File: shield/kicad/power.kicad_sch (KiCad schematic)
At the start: 89 parts, among them J1 USB_Micro-B, J2 Battery, J3 J3, J4 J4, J5 J5, J6 Conn_01x03, J7 PWR_GOOD, Q1 NTR4101PT1G, Q2 DMG1012T, Q3 DMG1012T, Q4 NTR4101PT1G, Q5 DMG1012T, Q6 DMG1012T, SW1 SW_Push, SW2 SW_SPDT, U1 BQ25060, U2 TPS3422, U3 STC3100, U4 TPS63060, U5 MAX803

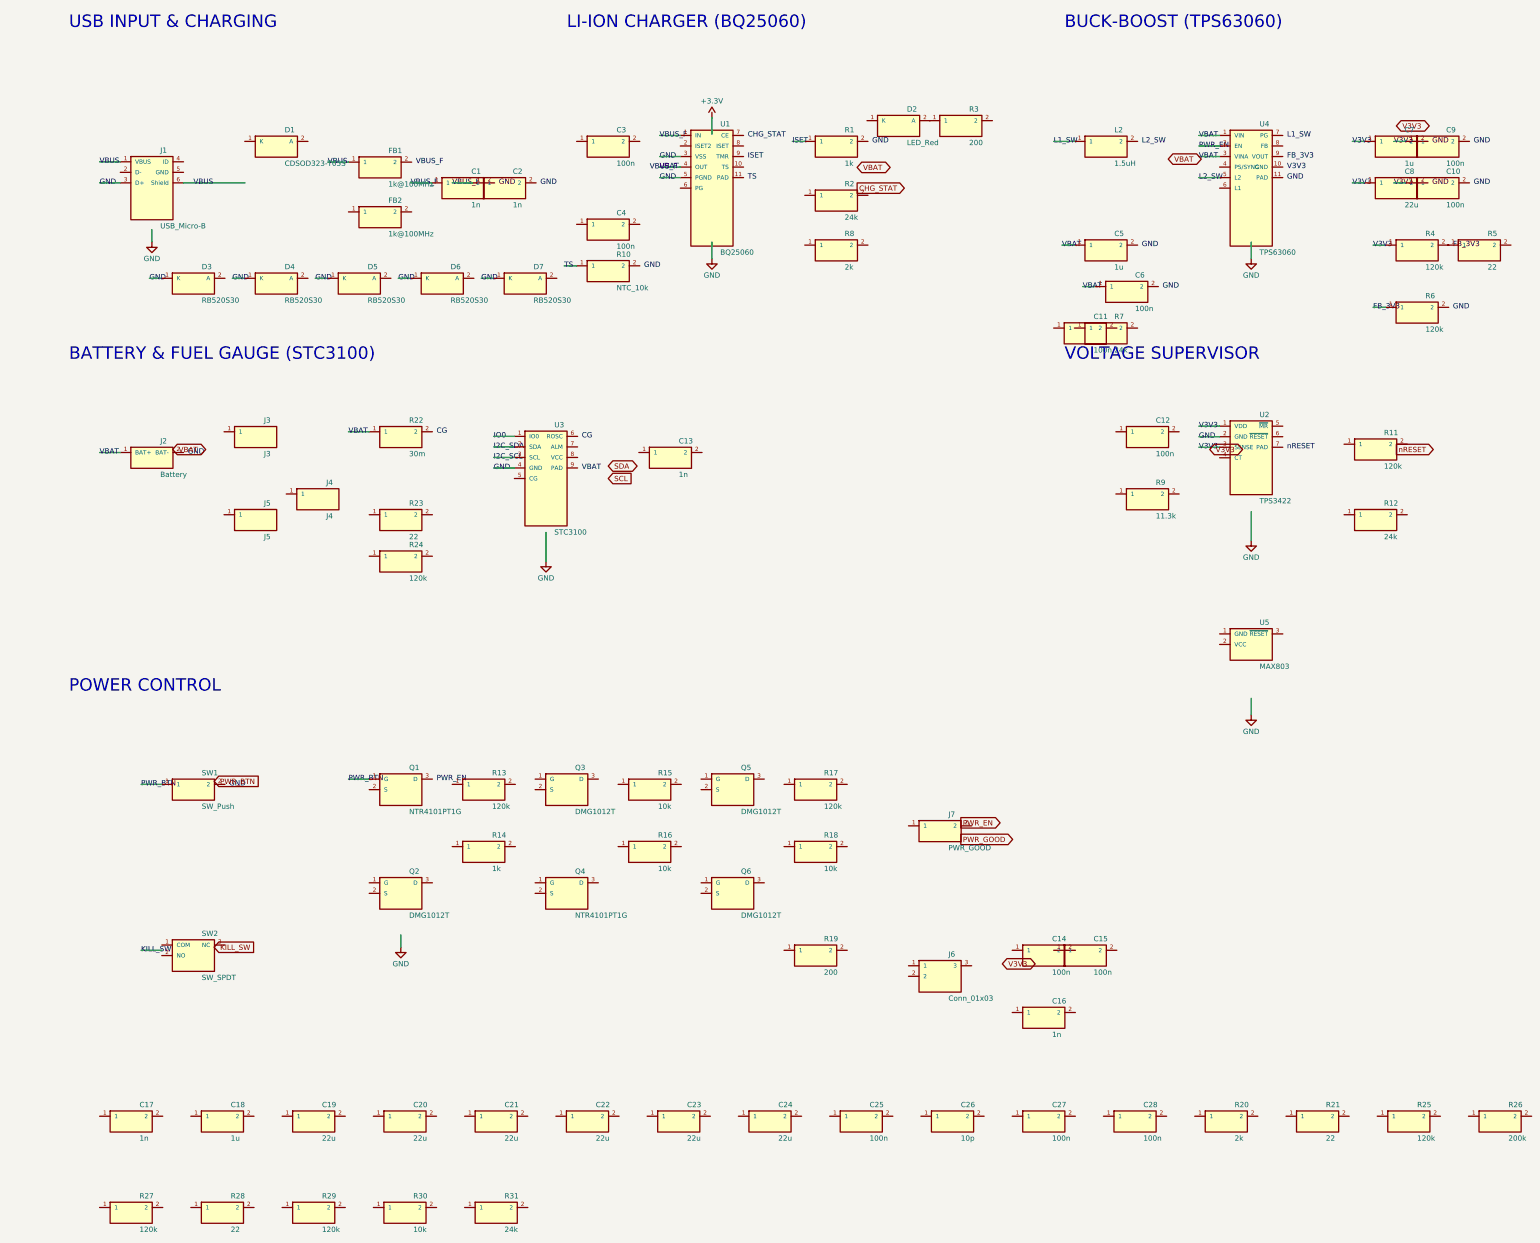
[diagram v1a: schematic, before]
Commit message: Add descriptive text blocks to all schematic sheets describing functional blocks
- Main sheet: board overview, sub-sheet summaries, and design notes
- Power sheet: USB input, charger, fuel gauge, buck-boost, supervisor, power control descriptions
- Peripherals sheet: smartcard, QR scanner, Arduino headers, buzzer, bypass descriptions
- Re-rendered all schematic and PCB images with kicad-cli-nightly

Agent-Logs-Url: https://github.com/3rdIteration/specter-diy/sessions/73613ef4-1004-4e39-bea0-e2793e248b2a

Co-authored-by: 3rdIteration <2230318+3rdIteration@users.noreply.github.com>
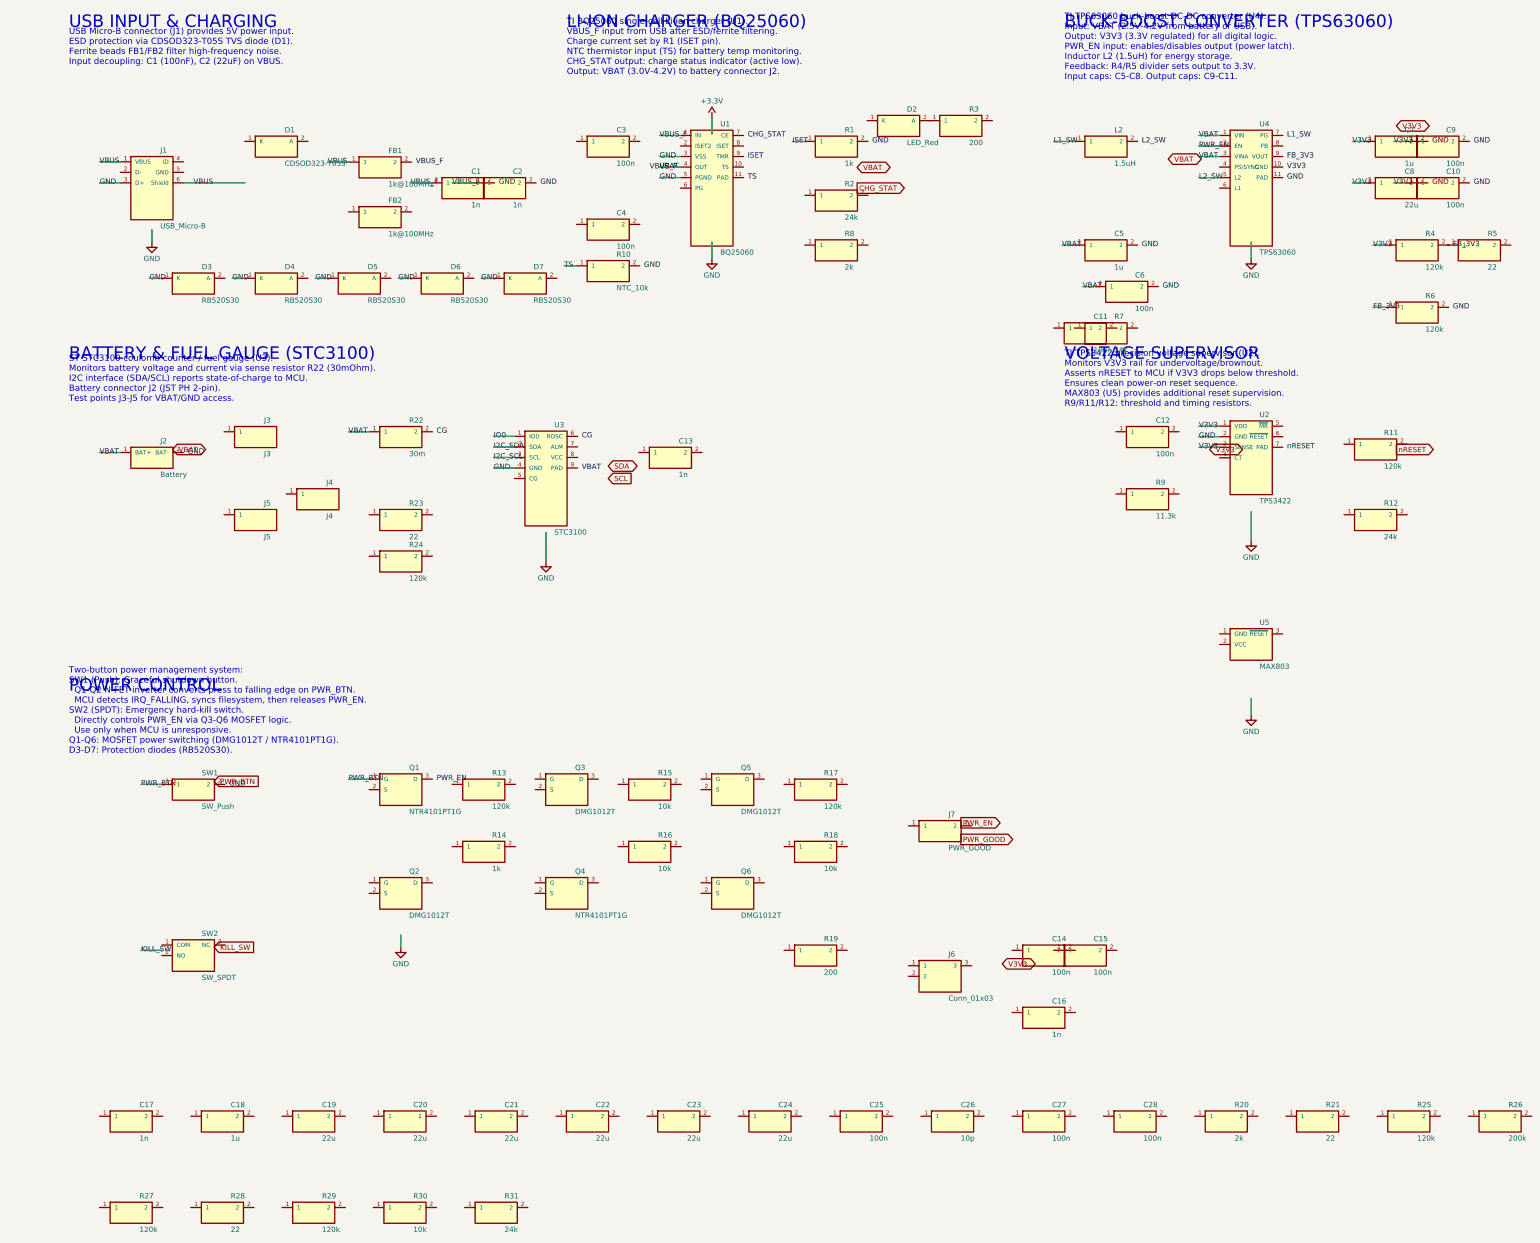
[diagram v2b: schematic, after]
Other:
- note added: "BUCK-BOOST CONVERTER (TPS63060)"
- note added: "ST STC3100 coulomb counter / fuel gauge (U3). Monitors battery voltage and current via sense resistor R22 (30mOhm). I2C interface (SDA/SCL) reports state-of-charge to MCU. Battery connector J2 (JST PH 2-pin). Test points J3-J5 for VBAT/GND access."
- note added: "TI BQ25060 single-cell Li-ion charger (U1). VBUS_F input from USB after ESD/ferrite filtering. Charge current set by R1 (ISET pin). NTC thermistor input (TS) for battery temp monitoring. CHG_STAT output: charge status indicator (active low). Output: VBAT (3.0V-4.2V) to battery connector J2."
- note added: "TI TPS3422 precision voltage supervisor (U2). Monitors V3V3 rail for undervoltage/brownout. Asserts nRESET to MCU if V3V3 drops below threshold. Ensures clean power-on reset sequence. MAX803 (U5) provides additional reset supervision. R9/R11/R12: threshold and timing resistors."
- note added: "TI TPS63060 buck-boost DC-DC converter (U4). Input: VBAT (2.5V-4.2V from battery or USB). Output: V3V3 (3.3V regulated) for all digital logic. PWR_EN input: enables/disables output (power latch). Inductor L2 (1.5uH) for energy storage. Feedback: R4/R5 divider sets output to 3.3V. Input caps: C5-C8. Output caps: C9-C11."
- note added: "Two-button power management system: SW1 (Push): Graceful shutdown button. Q1-Q2 N-FET inverter converts press to falling edge on PWR_BTN. MCU detects IRQ_FALLING, syncs filesystem, then releases PWR_EN. SW2 (SPDT): Emergency hard-kill switch. Directly controls PWR_EN via Q3-Q6 MOSFET logic. Use only when MCU is unresponsive. Q1-Q6: MOSFET power switching (DMG1012T / NTR4101PT1G). D3-D7: Protectio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"
- note added: "USB Micro-B connector (J1) provides 5V power input. ESD protection via CDSOD323-T05S TVS diode (D1). Ferrite beads FB1/FB2 filter high-frequency noise. Input decoupling: C1 (100nF), C2 (22uF) on VBUS."
- note removed: "BUCK-BOOST (TPS63060)"
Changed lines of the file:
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@@
 		(title "Specter Shield v1 - Power Supply")
 	)
-	(text "USB INPUT & CHARGING"
-		(exclude_from_sim no)
-		(at 25 25 0)
-		(effects
-			(font
-				(size 3 3)
-			)
-			(justify left)
-		)
-	)
-	(text "LI-ION CHARGER (BQ25060)"
-		(exclude_from_sim no)
-		(at 145 25 0)
-		(effects
-			(font
-				(size 3 3)
-			)
-			(justify left)
-		)
-	)
-	(text "BATTERY & FUEL GAUGE (STC3100)"
-		(exclude_from_sim no)
-		(at 25 105 0)
-		(effects
-			(font
-				(size 3 3)
-			)
-			(justify left)
-		)
-	)
-	(text "BUCK-BOOST (TPS63060)"
-		(exclude_from_sim no)
-		(at 265 25 0)
-		(effects
-			(font
-				(size 3 3)
-			)
-			(justify left)
-		)
-	)
-	(text "VOLTAGE SUPERVISOR"
-		(exclude_from_sim no)
-		(at 265 105 0)
-		(effects
-			(font
-				(size 3 3)
-			)
-			(justify left)
-		)
-	)
-	(text "POWER CONTROL"
-		(exclude_from_sim no)
-		(at 25 185 0)
-		(effects
-			(font
-				(size 3 3)
-			)
-			(justify left)
-		)
-	)
 	(wire
 		(pts
@@
 			)
 			(justify left)
+		)
+	)
+	(text "USB INPUT & CHARGING"
+		(exclude_from_sim no)
+		(at 25 25 0)
+		(effects
+			(font
+				(size 3 3)
+			)
+			(justify left)
+		)
+	)
+	(text "USB Micro-B connector (J1) provides 5V power input.\nESD protection via CDSOD323-T05S TVS diode (D1).\nFerrite beads FB1/FB2 filter high-frequency noise.\nInput decoupling: C1 (100nF), C2 (22uF) on VBUS."
+		(exclude_from_sim no)
+		(at 25 31 0)
+		(effects
+			(font
+				(size 1.5 1.5)
+				(color 0 0 150 1)
+			)
+			(justify left)
+		)
+	)
+	(text "LI-ION CHARGER (BQ25060)"
+		(exclude_from_sim no)
+		(at 145 25 0)
+		(effects
+			(font
+				(size 3 3)
+			)
+			(justify left)
+		)
+	)
+	(text "TI BQ25060 single-cell Li-ion charger (U1).\nVBUS_F input from USB after ESD/ferrite filtering.\nCharge current set by R1 (ISET pin).\nNTC thermistor input (TS) for battery temp monitoring.\nCHG_STAT output: charge status indicator (active low).\nOutput: VBAT (3.0V-4.2V) to battery connector J2."
+		(exclude_from_sim no)
+		(at 145 31 0)
+		(effects
+			(font
+				(size 1.5 1.5)
+				(color 0 0 150 1)
+			)
+			(justify left)
+		)
+	)
+	(text "BATTERY & FUEL GAUGE (STC3100)"
+		(exclude_from_sim no)
+		(at 25 105 0)
+		(effects
+			(font
+				(size 3 3)
+			)
+			(justify left)
+		)
+	)
+	(text "ST STC3100 coulomb counter / fuel gauge (U3).\nMonitors battery voltage and current via sense resistor R22 (30mOhm).\nI2C interface (SDA/SCL) reports state-of-charge to MCU.\nBattery connector J2 (JST PH 2-pin).\nTest points J3-J5 for VBAT/GND access."
+		(exclude_from_sim no)
+		(at 25 111 0)
+		(effects
+			(font
+				(size 1.5 1.5)
+				(color 0 0 150 1)
+			)
+			(justify left)
+		)
+	)
+	(text "BUCK-BOOST CONVERTER (TPS63060)"
+		(exclude_from_sim no)
+		(at 265 25 0)
+		(effects
+			(font
+				(size 3 3)
+			)
+			(justify left)
+		)
+	)
+	(text "TI TPS63060 buck-boost DC-DC converter (U4).\nInput: VBAT (2.5V-4.2V from battery or USB).\nOutput: V3V3 (3.3V regulated) for all digital logic.\nPWR_EN input: enables/disables output (power latch).\nInductor L2 (1.5uH) for energy storage.\nFeedback: R4/R5 divider sets output to 3.3V.\nInput caps: C5-C8. Output caps: C9-C11."
+		(exclude_from_sim no)
+		(at 265 31 0)
+		(effects
+			(font
+				(size 1.5 1.5)
+				(color 0 0 150 1)
+			)
+			(justify left)
+		)
+	)
+	(text "VOLTAGE SUPERVISOR"
+		(exclude_from_sim no)
+		(at 265 105 0)
+		(effects
+			(font
+				(size 3 3)
+			)
+			(justify left)
+		)
+	)
+	(text "TI TPS3422 precision voltage supervisor (U2).\nMonitors V3V3 rail for undervoltage/brownout.\nAsserts nRESET to MCU if V3V3 drops below threshold.\nEnsures clean power-on reset sequence.\nMAX803 (U5) provides additional reset supervision.\nR9/R11/R12: threshold and timing resistors."
+		(exclude_from_sim no)
+		(at 265 111 0)
+		(effects
+			(font
+				(size 1.5 1.5)
+				(color 0 0 150 1)
+			)
+			(justify left)
+		)
+	)
+	(text "POWER CONTROL"
+		(exclude_from_sim no)
+		(at 25 185 0)
+		(effects
+			(font
+				(size 3 3)
+			)
+			(justify left)
+		)
+	)
+	(text "Two-button power management system:\nSW1 (Push): Graceful shutdown button.\n  Q1-Q2 N-FET inverter converts press to falling edge on PWR_BTN.\n  MCU detects IRQ_FALLING, syncs filesystem, then releases PWR_EN.\nSW2 (SPDT): Emergency hard-kill switch.\n  Directly controls PWR_EN via Q3-Q6 MOSFET logic.\n  Use only when MCU is unresponsive.\nQ1-Q6: MOSFET power switching (DMG1012T / NTR4101PT1G).\nD3-D7: Protection diodes (RB520S30)."
+		(exclude_from_sim no)
+		(at 25 191 0)
+		(effects
+			(font
+				(size 1.5 1.5)
+				(color 0 0 150 1)
+			)
+			(justify left)

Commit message: Add LCSC part numbers to all shield schematic components and verify pinouts
Added LCSC properties to 127 components across both schematic sheets:
- power.kicad_sch: 83 components (lib_symbols + instances)
- structure_diagram.kicad_sch: 44 components (lib_symbols + instances)

All IC pinouts verified against manufacturer datasheets:
- BQ25060DQCR (U1): 10-pin DFN, pins match TI datasheet
- TPS63060DSCR (U4): 10-pin VSON, pins match TI datasheet
- STC3100IST (U3): 8-pin DFN, pins match ST datasheet
- TPS3422EGDRYR (U2): 6-pin DFN, pins match TI datasheet
- MAX803SQ293D2T1G (U5): 3-pin SOT-23, pins match onsemi datasheet
- ST8034HNQR (U6): 24-pin QFN, pins match ST datasheet
- NTR4101PT1G (Q1,Q4): SOT-23 P-ch MOSFET, G/S/D verified
- DMG1012T (Q2,Q3,Q5,Q6): SOT-523 N-ch MOSFET, G/S/D verified

2 ICs not available on LCSC (TPS3422, MAX803) - noted for manual sourcing.
Updated README with comprehensive LCSC BOM table.

Agent-Logs-Url: https://github.com/3rdIteration/specter-diy/sessions/22e4313c-030b-4d7a-a876-9de4f55077cb

Co-authored-by: 3rdIteration <2230318+3rdIteration@users.noreply.github.com>
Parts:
- C1, C13, C16, C17, C2: LCSC (none) -> C1560
- C10, C11, C12, C14, C15, C25, C27, C28, C3, C4, C6, C9: LCSC (none) -> C1525
- C18, C5, C7: LCSC (none) -> C307331
- C19, C20, C21, C22, C23, C24, C8: LCSC (none) -> C784585
- C26: LCSC (none) -> C1557
- D1: LCSC (none) -> C3706224
- D2: LCSC (none) -> C2286
- D3, D4, D5, D6, D7: LCSC (none) -> C167132
- FB1, FB2: LCSC (none) -> C1002
- J1: LCSC (none) -> C132560
- J2: LCSC (none) -> C295747
- J6: LCSC (none) -> C265101
- L2: LCSC (none) -> C49990
- Q1, Q4: LCSC (none) -> C35920
- Q2, Q3, Q5, Q6: LCSC (none) -> C42385153
- R1, R14: LCSC (none) -> C11702
- R10: LCSC (none) -> C525371
- R11, R13, R17, R24, R25, R27, R29, R4, R6: LCSC (none) -> C138051
- R12, R2, R31, R7: LCSC (none) -> C15749
- R15, R16, R18, R30: LCSC (none) -> C25804
- R19, R3: LCSC (none) -> C26083
- R20, R8: LCSC (none) -> C25794
- R21, R23, R28, R5: LCSC (none) -> C25092
- R22: LCSC (none) -> C23209
- R26: LCSC (none) -> C156444
- R9: LCSC (none) -> C15000
- SW1: LCSC (none) -> C221930
- SW2: LCSC (none) -> C226259
- U1: LCSC (none) -> C2835501
- U3: LCSC (none) -> C2969798
- U4: LCSC (none) -> C48567
